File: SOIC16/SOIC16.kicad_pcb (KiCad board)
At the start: 2 copper layers, 15.7 x 20.8 mm, 8 parts, among them J1 Conn_02x08_Counter_Clockwise, J2 Conn_01x08, J3 Conn_01x08

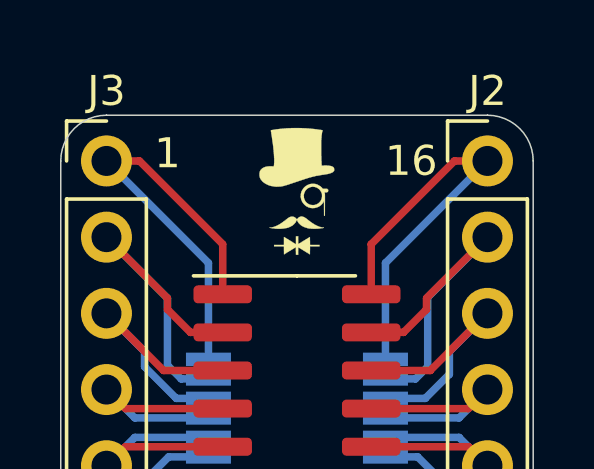
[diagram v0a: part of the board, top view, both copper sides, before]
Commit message: SOIC20 and SOIC28 Added
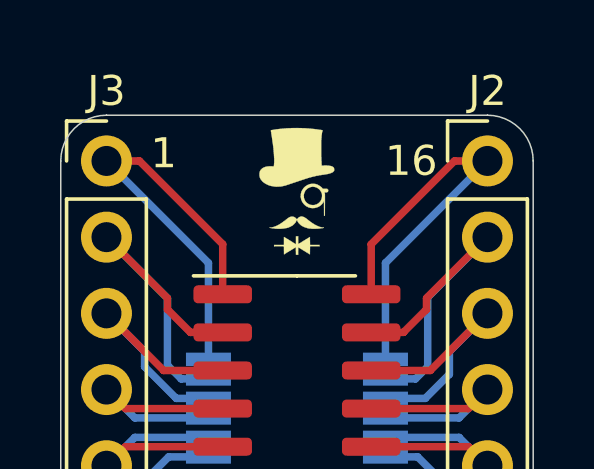
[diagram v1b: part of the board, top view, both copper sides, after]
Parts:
- moved G*** 1.02 mm to (194.3, 70.9)
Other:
- board text added: "www.SirBoard.com"
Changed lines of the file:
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@@
   (general
     (thickness 1.6)
-    (drawings 18)
+    (drawings 19)
     (tracks 92)
     (zones 0)
@@
   )
   (module logo:SirBoard60x21 (layer B.Cu)
-    (at 194.31 71.882)
+    (at 194.31 70.866)
     (fp_text reference G*** (at 0 0) (layer B.SilkS) hide
       (effects (font (size 1.524 1.524) (thickness 0.3)) (justify mirror))
@@
     )
   )
+  (gr_text www.SirBoard.com (at 194.31 73.152 180) (layer B.SilkS)
+    (effects (font (size 0.8 0.7) (thickness 0.15)) (justify mirror))
+  )
   (gr_line (start 202.184 71.12) (end 202.184 88.9) (layer Edge.Cuts) (width 0.05))
   (gr_line (start 187.96 69.596) (end 200.66 69.596) (layer Edge.Cuts) (width 0.05))
@@
     (effects (font (size 0.8 0.8) (thickness 0.15)))
   )
-  (gr_text 9 (at 198.12 71.12 180) (layer B.SilkS)
+  (gr_text 9 (at 198.755 70.993 180) (layer B.SilkS)
     (effects (font (size 1 1) (thickness 0.15)) (justify mirror))
   )
-  (gr_text 8 (at 189.992 70.866 180) (layer B.SilkS)
+  (gr_text 8 (at 189.738 70.866 180) (layer B.SilkS)
     (effects (font (size 1 1) (thickness 0.15)) (justify mirror))
   )
@@
     (effects (font (size 1 1) (thickness 0.15)))
   )
-  (gr_text 1 (at 189.992 70.866) (layer F.SilkS)
+  (gr_text 1 (at 189.865 70.866) (layer F.SilkS)
     (effects (font (size 1 1) (thickness 0.15)))
   )

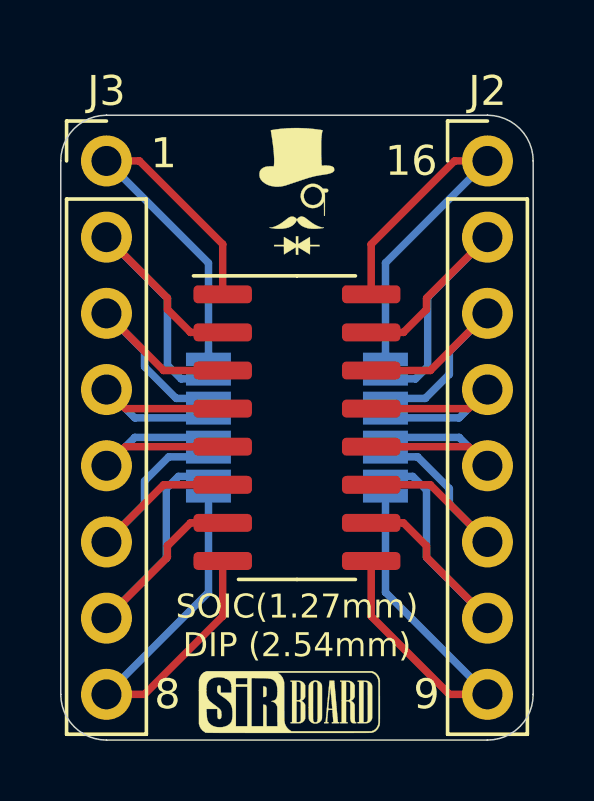
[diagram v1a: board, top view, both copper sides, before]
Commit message: Silkscreens and sizes updated
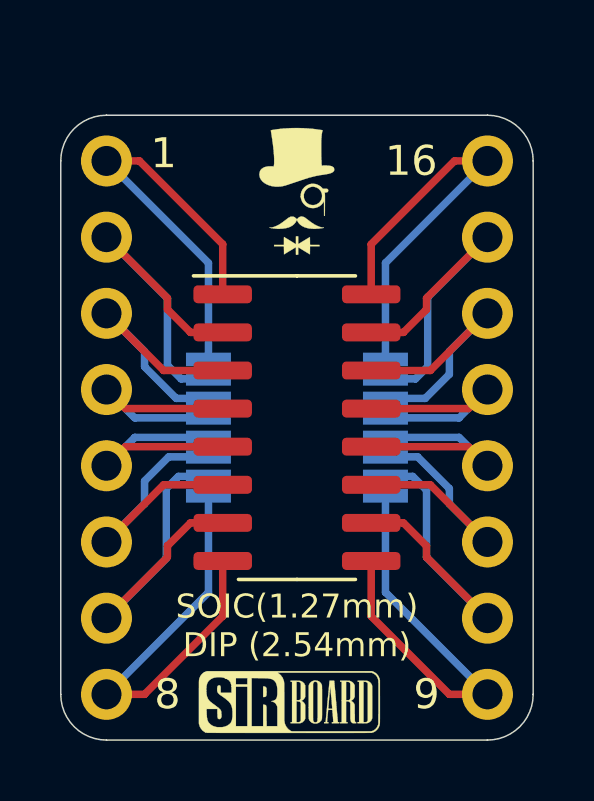
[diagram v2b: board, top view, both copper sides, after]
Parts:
- J2, J3: moved to B.Cu
- turned J2 to 180 degrees
- turned J3 to 180 degrees

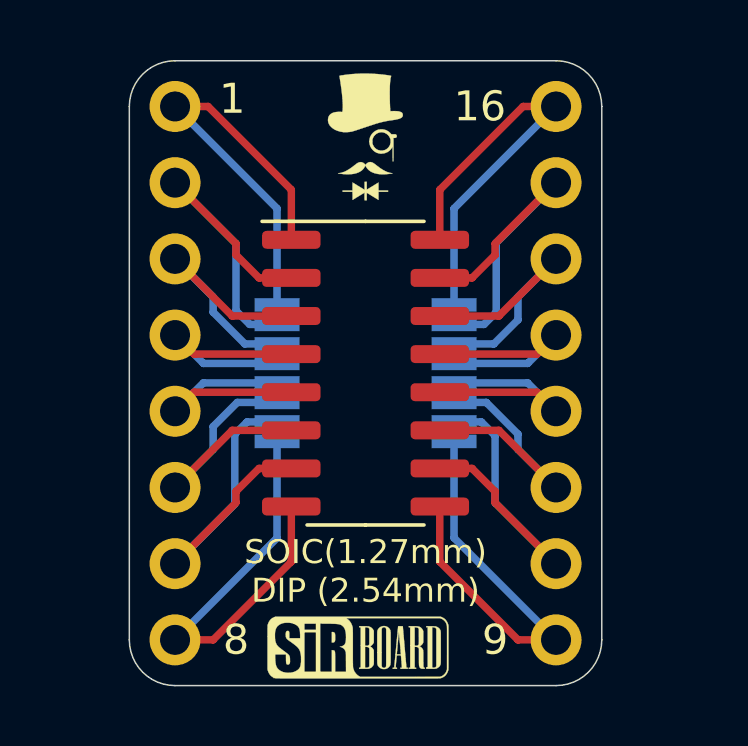
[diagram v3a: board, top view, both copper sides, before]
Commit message: Numbering Orientation Edited
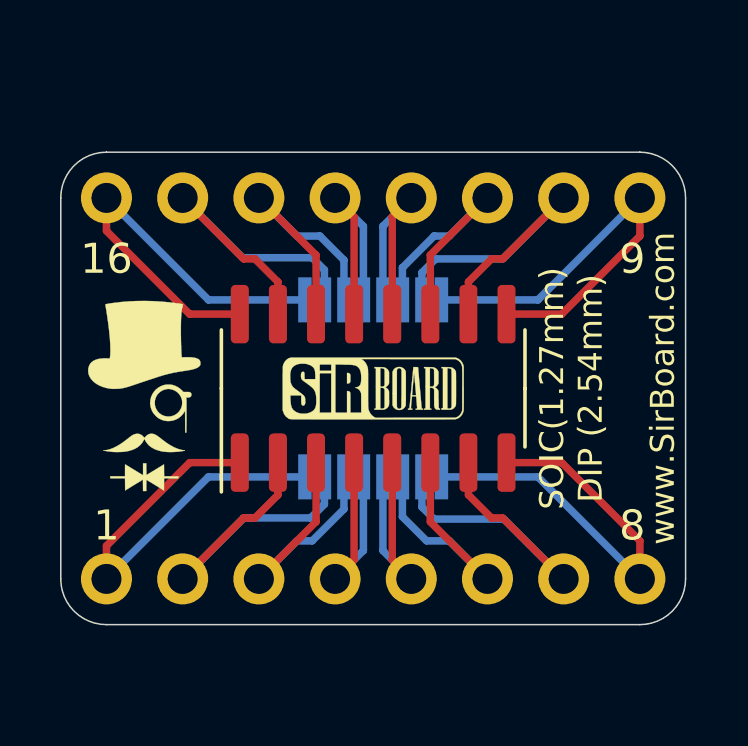
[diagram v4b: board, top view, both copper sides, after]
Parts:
- removed the G*** at (194.3, 72.1)
- added G***: LOGO, logo:logo63x89, F.Cu at (186.9, 80.8)
- J2, J3: moved to F.Cu
- moved J3 15.9 mm to (185.7, 86.9), turned to 90 degrees
- moved J2 15.3 mm to (185.7, 74.2), turned to 90 degrees
- moved G*** 13.0 mm to (185.7, 80.5), turned to 90 degrees
- moved G*** 8.82 mm to (200.9, 80.5), turned to 180 degrees
- moved G*** 8.65 mm to (194.6, 80.5)
- moved J1 0.57 mm to (194.6, 80.5), turned to 90 degrees
- moved REF** 0.57 mm to (194.6, 80.5), turned to 90 degrees
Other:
- board size 15.7 x 20.8 mm -> 20.8 x 15.7 mm

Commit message: Silkscreen Edits
Dimensions moved to Drawings Layer
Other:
- rule pad_to_mask_clearance: 0.051 -> 0
- rule solder_mask_min_width: 0.25 -> 0.1
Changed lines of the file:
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@@
     (pad_size 1.7 1.7)
     (pad_drill 1)
-    (pad_to_mask_clearance 0.051)
-    (solder_mask_min_width 0.25)
+    (pad_to_mask_clearance 0)
+    (solder_mask_min_width 0.1)
     (aux_axis_origin 0 0)
     (visible_elements 7FFFFFFF)
@@
       (usegerberadvancedattributes false)
       (creategerberjobfile false)
-      (excludeedgelayer false)
+      (excludeedgelayer true)
       (linewidth 0.100000)
       (plotframeref false)
       (viasonmask false)
       (mode 1)
-      (useauxorigin false)
+      (useauxorigin true)
       (hpglpennumber 1)
       (hpglpenspeed 20)
@@
       (drillshape 0)
       (scaleselection 1)
-      (outputdirectory "../../Gerbers/DIP16Adapter/"))
+      (outputdirectory "../../Gerbers/SOIC16/"))
   )
   (net 0 "")
@@
     (effects (font (size 0.8 0.8) (thickness 0.12)))
   )
-  (dimension 17.78 (width 0.15) (layer F.SilkS)
-    (gr_text "17.780 mm" (at 194.564 69.439) (layer F.SilkS)
+  (dimension 17.78 (width 0.15) (layer Dwgs.User)
+    (gr_text "17.780 mm" (at 194.564 69.439) (layer Dwgs.User)
       (effects (font (size 1 1) (thickness 0.15)) (justify mirror) hide)
     )
@@
     (arrow2b (pts (xy 185.674 70.739) (xy 186.800504 70.152579)))
   )
-  (dimension 12.7 (width 0.15) (layer F.SilkS)
-    (gr_text "12.700 mm" (at 181.834 80.518 90) (layer F.SilkS)
+  (dimension 12.7 (width 0.15) (layer Dwgs.User)
+    (gr_text "12.700 mm" (at 181.834 80.518 90) (layer Dwgs.User)
       (effects (font (size 1 1) (thickness 0.15)) (justify mirror) hide)
     )
@@
     (arrow2b (pts (xy 183.134 86.868) (xy 182.547579 85.741496)))
   )
-  (dimension 20.828 (width 0.15) (layer F.SilkS)
-    (gr_text "20.828 mm" (at 194.564 66.899) (layer F.SilkS)
+  (dimension 20.828 (width 0.15) (layer Dwgs.User)
+    (gr_text "20.828 mm" (at 194.564 66.899) (layer Dwgs.User)
       (effects (font (size 1 1) (thickness 0.15)) (justify mirror) hide)
     )
@@
     (arrow2b (pts (xy 184.15 68.199) (xy 185.276504 67.612579)))
   )
-  (dimension 15.748 (width 0.15) (layer F.SilkS)
-    (gr_text "15.748 mm" (at 178.99428 80.518 90) (layer F.SilkS)
+  (dimension 15.748 (width 0.15) (layer Dwgs.User)
+    (gr_text "15.748 mm" (at 178.99428 80.518 90) (layer Dwgs.User)
       (effects (font (size 1 1) (thickness 0.15)) (justify mirror) hide)
     )

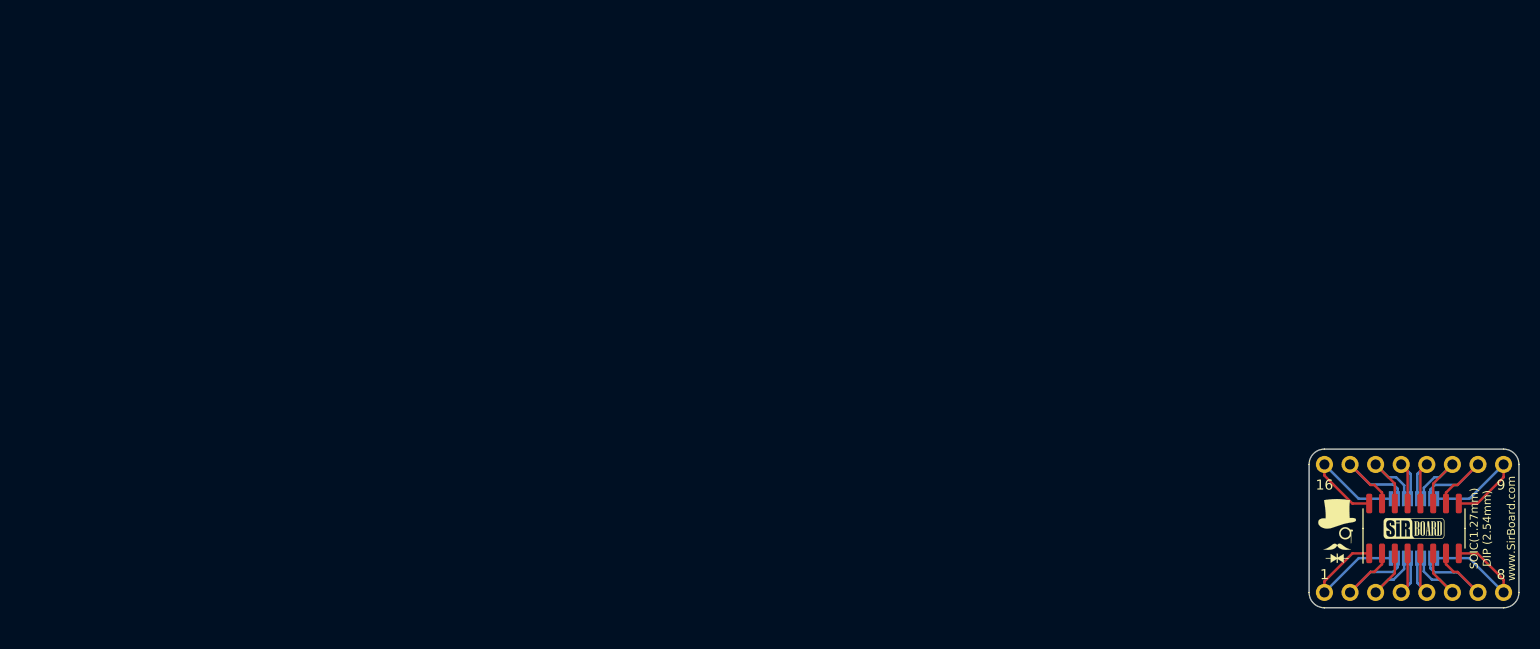
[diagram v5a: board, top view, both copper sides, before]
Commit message: USB, SD and CR Cells Added
MicroSD, MicroUSB, MiniUSB, USB-C, CR1220, CR2032 added as well as all schematics page sizes optimised
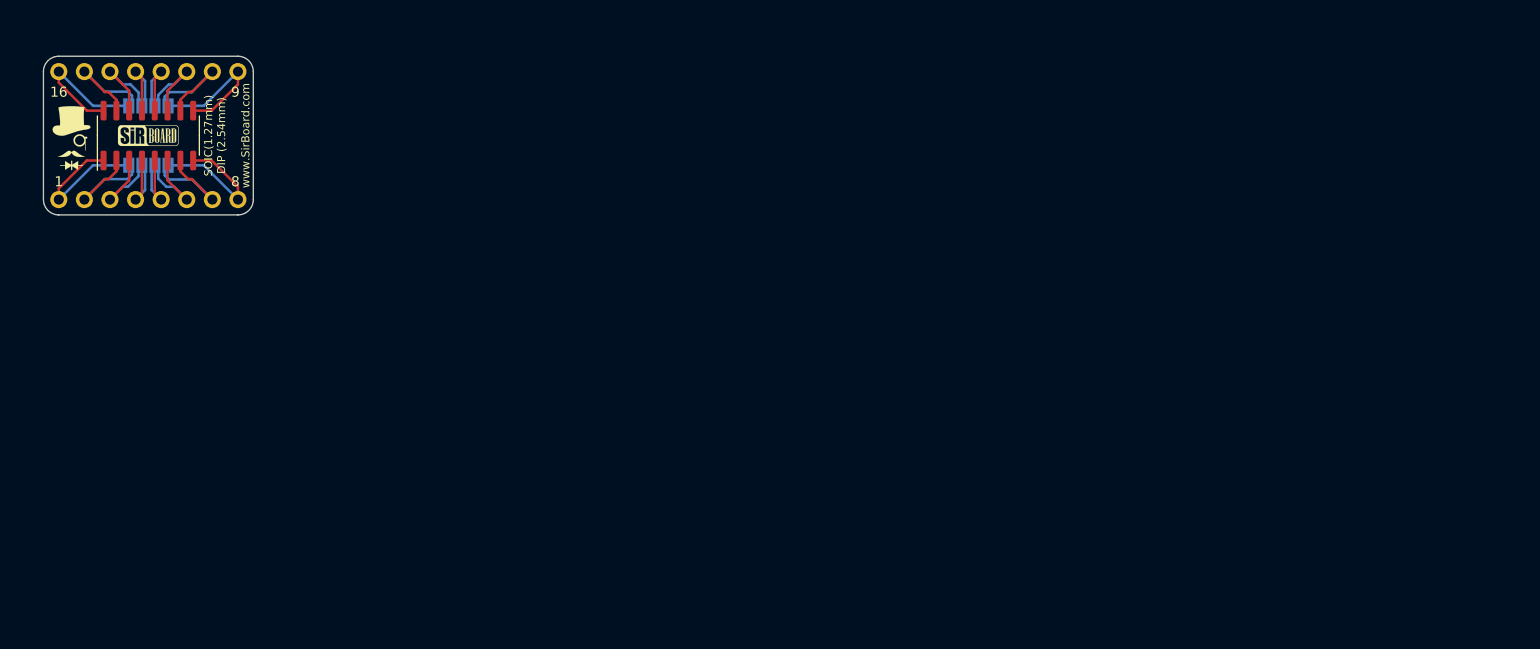
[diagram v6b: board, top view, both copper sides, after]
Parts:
- moved G*** 131.5 mm to (60.1, 41.5)
- moved J2 131.5 mm to (60.1, 35.2)
- moved J3 131.5 mm to (60.1, 47.9)
- moved G*** 131.5 mm to (61.3, 41.8)
- moved G*** 131.5 mm to (69.0, 41.5)
- moved G*** 131.5 mm to (75.3, 41.5)
- moved J1 131.5 mm to (69.0, 41.5)
- moved REF** 131.5 mm to (69.0, 41.5)

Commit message: Board Updates
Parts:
- G***: footprint logo:logo63x89 -> logo:logo54x76
- moved J3 6.84 mm to (57.5, 41.5)
- moved G*** 5.68 mm to (66.4, 36.4)
- moved J1 5.68 mm to (66.4, 36.4)
- moved REF** 5.68 mm to (66.4, 36.4)
- moved G*** 5.68 mm to (58.8, 36.7)
- moved G*** 5.46 mm to (73.0, 36.6), turned to 90 degrees
- moved G*** 5.16 mm to (59.2, 36.4)
- moved J2 4.58 mm to (57.5, 31.4)
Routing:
- net Net-(J1-Pad9): track 14.8 -> 8.84 mm, vias 0 -> 1
- net Net-(J1-Pad8): track 14.8 -> 8.84 mm, vias 0 -> 1
- net Net-(J1-Pad16): track 14.7 -> 8.84 mm, vias 0 -> 1
- net Net-(J1-Pad1): track 14.7 -> 8.84 mm, vias 0 -> 1
- net Net-(J1-Pad13): track 7.93 -> 5.39 mm
- net Net-(J1-Pad12): track 7.93 -> 5.39 mm
- net Net-(J1-Pad5): track 7.93 -> 5.39 mm
- net Net-(J1-Pad4): track 7.93 -> 5.39 mm
- net Net-(J1-Pad10): track 12.1 -> 14.6 mm, vias 0 -> 1
- net Net-(J1-Pad7): track 12.1 -> 14.6 mm, vias 0 -> 1
- net Net-(J1-Pad14): track 9.68 -> 7.93 mm, vias 0 -> 1
- net Net-(J1-Pad6): track 9.68 -> 7.93 mm, vias 0 -> 1
- net Net-(J1-Pad3): track 9.54 -> 7.93 mm, vias 0 -> 1
- net Net-(J1-Pad11): track 9.54 -> 7.93 mm, vias 0 -> 1
- net Net-(J1-Pad15): track 12.1 -> 13.4 mm, vias 0 -> 1
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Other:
- board size 20.8 x 15.7 mm -> 20.3 x 12.7 mm
- net class Default: clearance 0.2 -> 0.127; trace_width 0.25 -> 0.127; via_dia 0.8 -> 0.6; via_drill 0.4 -> 0.3
- rule trace_clearance: 0.2 -> 0.127
- rule trace_min: 0.2 -> 0.127
- board text added: "DIP=2.54mm SOIC=1.27mm"
- board text added: "DIP=2.54mm TSSOP=0.65mm"
- board text removed: "SOIC(1.27mm) DIP (2.54mm)"
- board text removed: "TSSOP(0.65mm) DIP (2.54mm)"
- board text removed: "www.SirBoard.com"

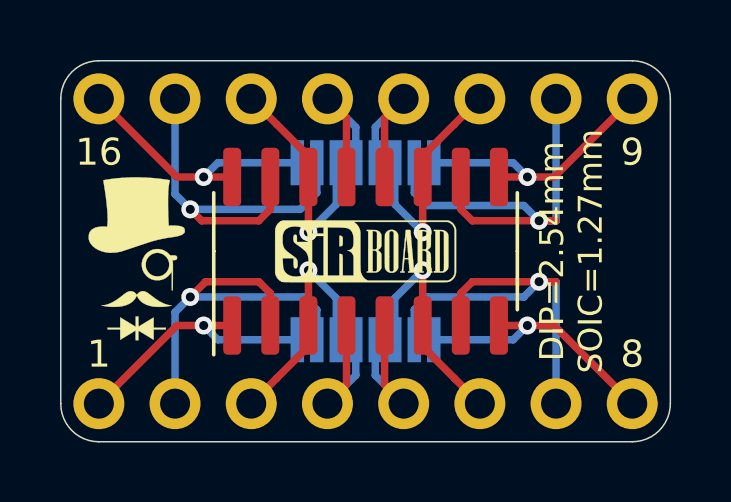
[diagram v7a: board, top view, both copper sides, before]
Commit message: Breakout Boards Revision 2
Renders updated, silkscreen text improved, blurry silkscreen items removed/resized.
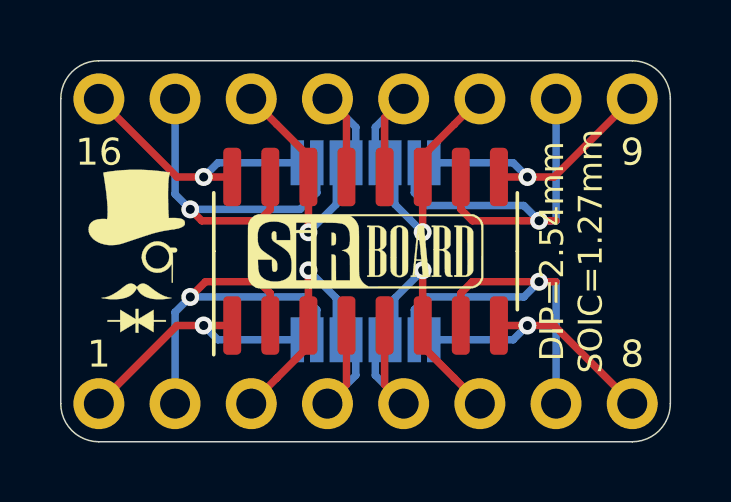
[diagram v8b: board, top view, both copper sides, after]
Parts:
- removed the G*** at (59.2, 36.4)
- G***: footprint logo:SirBoard60x21 -> logo:SirBoard79x25
- moved G*** 0.28 mm to (72.8, 36.4), turned to 180 degrees
- moved G*** 0.25 mm to (58.8, 36.4)
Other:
- board text added: "SirBoard.com"
